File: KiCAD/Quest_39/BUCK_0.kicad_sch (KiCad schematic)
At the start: 32 parts, among them U4 AD626ANZ, U5 INA226, U6 LTM4611EV-PBF, U7 MCP4151-502E/SN

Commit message: Gave all INA226's unique addresses
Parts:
- renumbered C20 to C19, C21 to C20, C22 to C21, C23 to C22, C24 to C23, C25 to C24, C26 to C25, C27 to C26, C28 to C27, R6 to R17, R7 to R18, R8 to R19, R9 to R20, R10 to R21, R11 to R22, R12 to R23, TP7 to TP6, TP6 to TP7
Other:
- note added: "Addr=0x40"
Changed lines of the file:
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@@
   (junction (at 203.2 50.8) (diameter 0) (color 0 0 0 0)
+  )
+  (junction (at 363.22 172.72) (diameter 0) (color 0 0 0 0)
   )
   (junction (at 67.31 50.8) (diameter 0) (color 0 0 0 0)
@@
     (stroke (width 0) (type default) (color 0 0 0 0))
   )
-  (wire (pts (xy 356.87 172.72) (xy 370.84 172.72))
+  (wire (pts (xy 356.87 172.72) (xy 363.22 172.72))
     (stroke (width 0) (type default) (color 0 0 0 0))
   )
@@
     (stroke (width 0) (type default) (color 0 0 0 0))
   )
+  (wire (pts (xy 363.22 172.72) (xy 370.84 172.72))
+    (stroke (width 0) (type default) (color 0 0 0 0))
+  )
   (wire (pts (xy 233.68 215.9) (xy 236.22 215.9))
     (stroke (width 0) (type default) (color 0 0 0 0))
@@
   (polyline (pts (xy 13.97 43.18) (xy 87.63 43.18))
     (stroke (width 0) (type default) (color 0 0 0 0))
+  )
+  (text "Addr=0x40" (at 102.87 92.71 0)
+    (effects (font (size 1.27 1.27)) (justify left bottom))
   )
   (text "10:1 divider" (at 26.67 69.85 0)
@@
   (symbol (lib_id "Device:C") (at 25.4 93.98 0) (unit 1)
     (in_bom yes) (on_board yes) (fields_autoplaced)
-    (property "Reference" "C20" (id 0) (at 29.21 92.7099 0)
+    (property "Reference" "C19" (id 0) (at 29.21 92.7099 0)
       (effects (font (size 1.27 1.27)) (justify left))
     )
@@
   (symbol (lib_id "Device:R") (at 129.54 100.33 0) (unit 1)
     (in_bom yes) (on_board yes) (fields_autoplaced)
-    (property "Reference" "R11" (id 0) (at 132.08 99.0599 0)
+    (property "Reference" "R22" (id 0) (at 132.08 99.0599 0)
       (effects (font (size 1.27 1.27)) (justify left))
     )
@@
   (symbol (lib_id "power:GND") (at 21.59 86.36 0) (unit 1)
     (in_bom yes) (on_board yes)
-    (property "Reference" "#PWR011" (id 0) (at 21.59 92.71 0)
+    (property "Reference" "#PWR032" (id 0) (at 21.59 92.71 0)
       (effects (font (size 1.27 1.27)) hide)
     )
@@
   (symbol (lib_id "power:GND") (at 116.84 110.49 0) (unit 1)
     (in_bom yes) (on_board yes)
-    (property "Reference" "#PWR0113" (id 0) (at 116.84 116.84 0)
+    (property "Reference" "#PWR035" (id 0) (at 116.84 116.84 0)
       (effects (font (size 1.27 1.27)) hide)
     )
@@
   (symbol (lib_id "Device:R") (at 25.4 64.77 0) (unit 1)
     (in_bom yes) (on_board yes) (fields_autoplaced)
-    (property "Reference" "R9" (id 0) (at 27.94 63.4999 0)
+    (property "Reference" "R20" (id 0) (at 27.94 63.4999 0)
       (effects (font (size 1.27 1.27)) (justify left))
     )
@@
   (symbol (lib_id "power:+5V") (at 93.98 81.28 0) (unit 1)
     (in_bom yes) (on_board yes) (fields_autoplaced)
-    (property "Reference" "#PWR0110" (id 0) (at 93.98 85.09 0)
+    (property "Reference" "#PWR030" (id 0) (at 93.98 85.09 0)
       (effects (font (size 1.27 1.27)) hide)
     )
@@
   (symbol (lib_id "power:GND") (at 340.36 238.76 0) (unit 1)
     (in_bom yes) (on_board yes) (fields_autoplaced)
-    (property "Reference" "#PWR0114" (id 0) (at 340.36 245.11 0)
+    (property "Reference" "#PWR038" (id 0) (at 340.36 245.11 0)
       (effects (font (size 1.27 1.27)) hide)
     )
@@
   (symbol (lib_id "Connector:TestPoint") (at 234.95 53.34 0) (unit 1)
     (in_bom yes) (on_board yes)
-    (property "Reference" "TP7" (id 0) (at 234.95 48.26 0)
+    (property "Reference" "TP6" (id 0) (at 234.95 48.26 0)
       (effects (font (size 1.27 1.27)) (justify left))
     )
@@
   (symbol (lib_id "Device:R") (at 67.31 63.5 0) (unit 1)
     (in_bom yes) (on_board yes)
-    (property "Reference" "R7" (id 0) (at 68.58 62.23 0)
+    (property "Reference" "R18" (id 0) (at 68.58 62.23 0)
       (effects (font (size 1.27 1.27)) (justify left))
     )
@@
   (symbol (lib_id "power:+5V") (at 340.36 227.33 0) (unit 1)
     (in_bom yes) (on_board yes) (fields_autoplaced)
-    (property "Reference" "#PWR0115" (id 0) (at 340.36 231.14 0)
+    (property "Reference" "#PWR036" (id 0) (at 340.36 231.14 0)
       (effects (font (size 1.27 1.27)) hide)
     )
@@
   (symbol (lib_id "Device:R") (at 25.4 74.93 0) (unit 1)
     (in_bom yes) (on_board yes) (fields_autoplaced)
-    (property "Reference" "R10" (id 0) (at 27.94 73.6599 0)
+    (property "Reference" "R21" (id 0) (at 27.94 73.6599 0)
       (effects (font (size 1.27 1.27)) (justify left))
     )
@@
   (symbol (lib_id "power:+5V") (at 64.77 83.82 0) (unit 1)
     (in_bom yes) (on_board yes) (fields_autoplaced)
-    (property "Reference" "#PWR010" (id 0) (at 64.77 87.63 0)
+    (property "Reference" "#PWR031" (id 0) (at 64.77 87.63 0)
       (effects (font (size 1.27 1.27)) hide)
     )
@@
   (symbol (lib_id "Device:R") (at 82.55 63.5 0) (unit 1)
     (in_bom yes) (on_board yes)
-    (property "Reference" "R8" (id 0) (at 78.74 62.23 0)
+    (property "Reference" "R19" (id 0) (at 78.74 62.23 0)
       (effects (font (size 1.27 1.27)) (justify left))
     )
@@
   (symbol (lib_id "Device:C_Polarized") (at 370.84 179.07 0) (unit 1)
     (in_bom yes) (on_board yes)
-    (property "Reference" "C24" (id 0) (at 374.6295 177.7575 0)
+    (property "Reference" "C23" (id 0) (at 374.6295 177.7575 0)
       (effects (font (size 1.27 1.27)) (justify left))
     )
@@
   (symbol (lib_id "Device:C") (at 344.17 181.61 0) (unit 1)
     (in_bom yes) (on_board yes)
-    (property "Reference" "C27" (id 0) (at 346.71 180.34 0)
+    (property "Reference" "C26" (id 0) (at 346.71 180.34 0)
       (effects (font (size 1.27 1.27)) (justify left))
     )
@@
   (symbol (lib_id "Device:C_Polarized") (at 396.24 179.07 0) (unit 1)
     (in_bom yes) (on_board yes)
-    (property "Reference" "C26" (id 0) (at 400.0295 177.7575 0)
+    (property "Reference" "C25" (id 0) (at 400.0295 177.7575 0)
       (effects (font (size 1.27 1.27)) (justify left))
     )
@@
     (pin "1")
     (pin "2")
+  )
+  (symbol (lib_id "power:PWR_FLAG") (at 363.22 172.72 0) (unit 1)
+    (in_bom yes) (on_board yes) (fields_autoplaced)
+    (property "Reference" "#FLG0102" (id 0) (at 363.22 170.815 0)
+      (effects (font (size 1.27 1.27)) hide)
+    )
+    (property "Value" "PWR_FLAG" (id 1) (at 363.22 167.64 0))
+    (property "Footprint" "" (id 2) (at 363.22 172.72 0)
+      (effects (font (size 1.27 1.27)) hide)
+    )
+    (property "Datasheet" "~" (id 3) (at 363.22 172.72 0)
+      (effects (font (size 1.27 1.27)) hide)
+    )
+    (pin "1")
   )
   (symbol (lib_id "AD626ANZ:AD626ANZ") (at 5.08 80.01 0) (unit 1)
@@
   (symbol (lib_id "Connector:TestPoint") (at 77.47 100.33 180) (unit 1)
     (in_bom yes) (on_board yes)
-    (property "Reference" "TP6" (id 0) (at 78.74 102.87 0)
+    (property "Reference" "TP7" (id 0) (at 78.74 102.87 0)
       (effects (font (size 1.27 1.27)) (justify right))
     )
@@
   (symbol (lib_id "Device:C") (at 63.5 95.25 0) (unit 1)
     (in_bom yes) (on_board yes)
-    (property "Reference" "C21" (id 0) (at 57.15 93.98 0)
+    (property "Reference" "C20" (id 0) (at 57.15 93.98 0)
       (effects (font (size 1.27 1.27)) (justify left))
     )
@@
   (symbol (lib_id "power:GND") (at 285.75 238.76 0) (unit 1)
     (in_bom yes) (on_board yes) (fields_autoplaced)
-    (property "Reference" "#PWR0116" (id 0) (at 285.75 245.11 0)
+    (property "Reference" "#PWR037" (id 0) (at 285.75 245.11 0)
       (effects (font (size 1.27 1.27)) hide)
     )
@@
   (symbol (lib_id "Device:C_Polarized") (at 383.54 179.07 0) (unit 1)
     (in_bom yes) (on_board yes)
-    (property "Reference" "C25" (id 0) (at 387.3295 177.7575 0)
+    (property "Reference" "C24" (id 0) (at 387.3295 177.7575 0)
       (effects (font (size 1.27 1.27)) (justify left))
     )
@@
   (symbol (lib_id "power:GND") (at 25.4 99.06 0) (unit 1)
     (in_bom yes) (on_board yes)
-    (property "Reference" "#PWR012" (id 0) (at 25.4 105.41 0)
+    (property "Reference" "#PWR033" (id 0) (at 25.4 105.41 0)
       (effects (font (size 1.27 1.27)) hide)
     )
@@
   (symbol (lib_id "Device:C_Polarized") (at 356.87 179.07 0) (unit 1)
     (in_bom yes) (on_board yes)
-    (property "Reference" "C23" (id 0) (at 360.6595 177.7575 0)
+    (property "Reference" "C22" (id 0) (at 360.6595 177.7575 0)
       (effects (font (size 1.27 1.27)) (justify left))
     )
@@
   (symbol (lib_id "Device:R") (at 74.93 50.8 90) (unit 1)
     (in_bom yes) (on_board yes)
-    (property "Reference" "R6" (id 0) (at 74.93 45.72 90))
+    (property "Reference" "R17" (id 0) (at 74.93 45.72 90))
     (property "Value" "0R0025" (id 1) (at 74.93 48.26 90))
     (property "Footprint" "" (id 2) (at 74.93 52.578 90)
@@
   (symbol (lib_id "Device:C") (at 105.41 137.16 0) (unit 1)
     (in_bom yes) (on_board yes) (fields_autoplaced)
-    (property "Reference" "C22" (id 0) (at 109.22 135.8899 0)
+    (property "Reference" "C21" (id 0) (at 109.22 135.8899 0)
       (effects (font (size 1.27 1.27)) (justify left))
     )
@@
   (symbol (lib_id "Device:C") (at 340.36 233.68 0) (unit 1)
     (in_bom yes) (on_board yes) (fields_autoplaced)
-    (property "Reference" "C28" (id 0) (at 344.17 232.4099 0)
+    (property "Reference" "C27" (id 0) (at 344.17 232.4099 0)
       (effects (font (size 1.27 1.27)) (justify left))
     )
@@
   (symbol (lib_id "power:PWR_FLAG") (at 166.37 50.8 0) (unit 1)
     (in_bom yes) (on_board yes) (fields_autoplaced)
-    (property "Reference" "#FLG0101" (id 0) (at 166.37 48.895 0)
+    (property "Reference" "#FLG03" (id 0) (at 166.37 48.895 0)
       (effects (font (size 1.27 1.27)) hide)
     )
@@
   (symbol (lib_id "power:GND") (at 63.5 100.33 0) (unit 1)
     (in_bom yes) (on_board yes)
-    (property "Reference" "#PWR013" (id 0) (at 63.5 106.68 0)
+    (property "Reference" "#PWR034" (id 0) (at 63.5 106.68 0)
       (effects (font (size 1.27 1.27)) hide)
     )
@@
   (symbol (lib_id "Device:R") (at 325.12 224.79 0) (unit 1)
     (in_bom yes) (on_board yes) (fields_autoplaced)
-    (property "Reference" "R12" (id 0) (at 327.66 223.5199 0)
-      (effects (font (size 1.27 1.27)) (justify left))
-    )
+    (property "Reference" "R23" (id 0) (at 327.66 223.5199 0)
+      (effects (font (size 1.27 1.27)) (justify left))
+    )

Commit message: Removed all ERC errors
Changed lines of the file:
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@@
   (junction (at 203.2 50.8) (diameter 0) (color 0 0 0 0)
-  )
-  (junction (at 363.22 172.72) (diameter 0) (color 0 0 0 0)
   )
   (junction (at 67.31 50.8) (diameter 0) (color 0 0 0 0)
@@
     (stroke (width 0) (type default) (color 0 0 0 0))
   )
-  (wire (pts (xy 356.87 172.72) (xy 363.22 172.72))
+  (wire (pts (xy 356.87 172.72) (xy 370.84 172.72))
     (stroke (width 0) (type default) (color 0 0 0 0))
   )
@@
   )
   (wire (pts (xy 63.5 99.06) (xy 63.5 100.33))
-    (stroke (width 0) (type default) (color 0 0 0 0))
-  )
-  (wire (pts (xy 363.22 172.72) (xy 370.84 172.72))
     (stroke (width 0) (type default) (color 0 0 0 0))
   )
@@
     (pin "2")
   )
-  (symbol (lib_id "power:PWR_FLAG") (at 363.22 172.72 0) (unit 1)
-    (in_bom yes) (on_board yes) (fields_autoplaced)
-    (property "Reference" "#FLG0102" (id 0) (at 363.22 170.815 0)
-      (effects (font (size 1.27 1.27)) hide)
-    )
-    (property "Value" "PWR_FLAG" (id 1) (at 363.22 167.64 0))
-    (property "Footprint" "" (id 2) (at 363.22 172.72 0)
-      (effects (font (size 1.27 1.27)) hide)
-    )
-    (property "Datasheet" "~" (id 3) (at 363.22 172.72 0)
-      (effects (font (size 1.27 1.27)) hide)
-    )
-    (pin "1")
-  )
   (symbol (lib_id "AD626ANZ:AD626ANZ") (at 5.08 80.01 0) (unit 1)

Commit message: Assigned all schem. symbols their footprints
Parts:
- removed C22, C23, C24, C25: 100uF, symbol Device:C_Polarized
- added C22, C23, C24, C25: 100uF, Capacitor_SMD:C_1206_3216Metric, symbol Device:C
- C14: footprint (none) -> Capacitor_SMD:CP_Elec_8x6.9
- C15, C16, C17, C19, C20, C21, C26, C27: footprint (none) -> Capacitor_SMD:C_0805_2012Metric
- C18: footprint OptoDevice:R_LDR_4.9x4.2mm_P2.54mm_Vertical -> Capacitor_SMD:C_0805_2012Metric
- R17: footprint (none) -> Resistor_SMD:R_1206_3216Metric
- R18, R19, R20, R21, R22, R23: footprint (none) -> Resistor_SMD:R_0805_2012Metric
- TP10, TP11, TP12, TP6, TP7, TP8, TP9: footprint (none) -> TestPoint:TestPoint_Pad_D2.0mm
- U4: footprint N_8_ADI -> Package_DIP:DIP-8_W7.62mm_Socket_LongPads
- U6: footprint LGA-133_3_LIT -> Package_LGA:Linear_LGA-133_15.0x15.0mm_Layout12x12_P1.27mm
- U7: footprint SOIC8-N_MC_MCH -> Package_SO:MSOP-8_3x3mm_P0.65mm
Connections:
- net NEG: now also C22.2, C23.2, C24.2, C25.2
- net POS: now also C22.1, C23.1, C24.1, C25.1

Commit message: Initial work on layout
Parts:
- C18, C19, C20, C21, C26, C27: footprint Capacitor_SMD:C_0805_2012Metric -> Capacitor_SMD:C_0603_1608Metric
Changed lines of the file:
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@@
       (effects (font (size 1.27 1.27)) (justify left))
     )
-    (property "Footprint" "Capacitor_SMD:C_0805_2012Metric" (id 2) (at 26.3652 97.79 0)
+    (property "Footprint" "Capacitor_SMD:C_0603_1608Metric" (id 2) (at 26.3652 97.79 0)
       (effects (font (size 1.27 1.27)) hide)
     )
@@
       (effects (font (size 1.27 1.27)) (justify left))
     )
-    (property "Footprint" "Capacitor_SMD:C_0805_2012Metric" (id 2) (at 345.1352 185.42 0)
+    (property "Footprint" "Capacitor_SMD:C_0603_1608Metric" (id 2) (at 345.1352 185.42 0)
       (effects (font (size 1.27 1.27)) hide)
     )
@@
     (property "Reference" "C18" (id 0) (at 74.93 73.66 90))
     (property "Value" "1uF" (id 1) (at 74.93 81.28 90))
-    (property "Footprint" "Capacitor_SMD:C_0805_2012Metric" (id 2) (at 78.74 76.5048 0)
+    (property "Footprint" "Capacitor_SMD:C_0603_1608Metric" (id 2) (at 78.74 76.5048 0)
       (effects (font (size 1.27 1.27)) hide)
     )
@@
       (effects (font (size 1.27 1.27)) (justify left))
     )
-    (property "Footprint" "Capacitor_SMD:C_0805_2012Metric" (id 2) (at 64.4652 99.06 0)
+    (property "Footprint" "Capacitor_SMD:C_0603_1608Metric" (id 2) (at 64.4652 99.06 0)
       (effects (font (size 1.27 1.27)) hide)
     )
@@
       (effects (font (size 1.27 1.27)) (justify left))
     )
-    (property "Footprint" "Capacitor_SMD:C_0805_2012Metric" (id 2) (at 106.3752 140.97 0)
+    (property "Footprint" "Capacitor_SMD:C_0603_1608Metric" (id 2) (at 106.3752 140.97 0)
       (effects (font (size 1.27 1.27)) hide)
     )
@@
       (effects (font (size 1.27 1.27)) (justify left))
     )
-    (property "Footprint" "Capacitor_SMD:C_0805_2012Metric" (id 2) (at 341.3252 237.49 0)
-      (effects (font (size 1.27 1.27)) hide)
-    )
+    (property "Footprint" "Capacitor_SMD:C_0603_1608Metric" (id 2) (at 341.3252 237.49 0)
+      (effects (font (size 1.27 1.27)) hide)
+    )

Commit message: Fixed INA226 schem. mistake and further layout work
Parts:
- added C19: 100nF, Capacitor_SMD:C_0603_1608Metric, symbol Device:C
- renumbered C19 to C20, C20 to C21, C21 to C22, C22 to C23, C23 to C24, C24 to C25, C25 to C26, C26 to C27, C27 to C28
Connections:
- net +5V: now also C19.1
- net GND: now also C19.2
- net PV_POS: no longer C14.1, C15.1, C16.1, C17.1, R17.2, R19.1, R22.1, U6.A1 (VIN), U6.A2 (VIN), U6.A3 (VIN), U6.A4 (VIN), U6.A5 (VIN), U6.A6 (VIN), U6.B1 (VIN), U6.B2 (VIN), U6.B3 (VIN), U6.B4 (VIN), U6.B5 (VIN), U6.B6 (VIN), U6.C1 (VIN), U6.C2 (VIN), U6.C3 (VIN), U6.C4 (VIN), U6.C5 (VIN), U6.C6 (VIN)
- net Vin+: now also C18.2; no longer C18.1
- net Vin-: now also C18.1; no longer C18.2, TP7.1, U4.5 (OUT), U5.8 (Vbus)
- new net: TP7.1, U4.5 (OUT), U5.8 (Vbus)
- new net BUCK_VIN: C14.1, C15.1, C16.1, C17.1, R17.2, R19.1, R22.1, U6.A1 (VIN), U6.A2 (VIN), U6.A3 (VIN), U6.A4 (VIN), U6.A5 (VIN), U6.A6 (VIN), U6.B1 (VIN), U6.B2 (VIN), U6.B3 (VIN), U6.B4 (VIN), U6.B5 (VIN), U6.B6 (VIN), U6.C1 (VIN), U6.C2 (VIN), U6.C3 (VIN), U6.C4 (VIN), U6.C5 (VIN), U6.C6 (VIN)
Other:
- moved on the sheet: C18

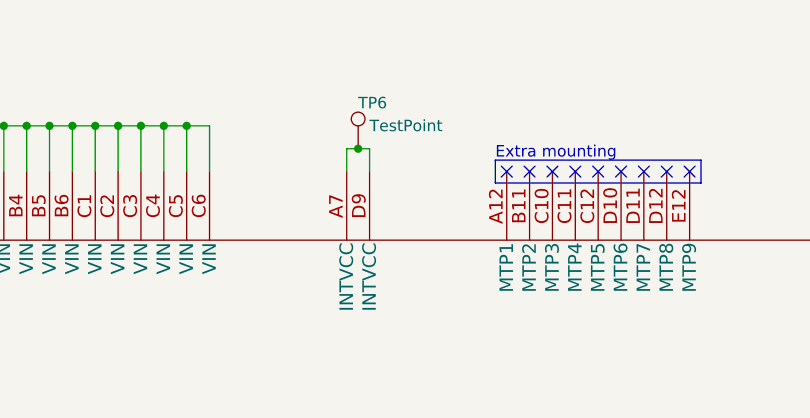
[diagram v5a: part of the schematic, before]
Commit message: Partial wiring of first buck converter section PCB layout
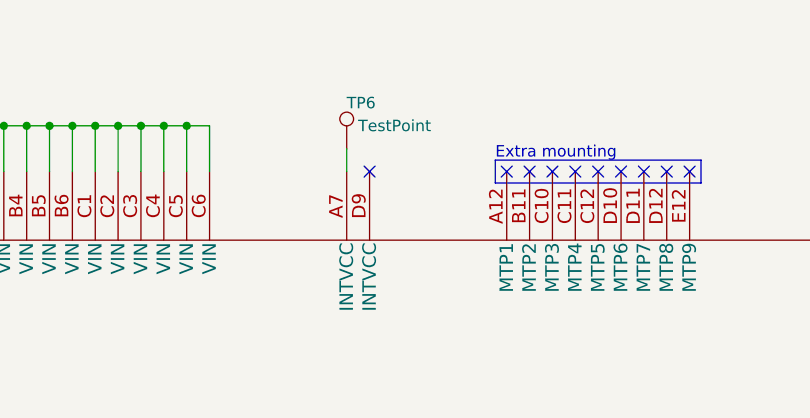
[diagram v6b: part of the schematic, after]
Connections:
- net at TP6.1, U6.A7 (INTVCC): no longer U6.D9 (INTVCC)
- no-connect marks 12 -> 13
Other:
- moved on the sheet: TP6
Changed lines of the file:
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@@
   (junction (at 130.81 50.8) (diameter 0) (color 0 0 0 0)
-  )
-  (junction (at 234.95 53.34) (diameter 0) (color 0 0 0 0)
   )
   (junction (at 279.4 215.9) (diameter 0) (color 0 0 0 0)
@@
   (no_connect (at 259.08 55.88))
   (no_connect (at 266.7 55.88))
+  (no_connect (at 236.22 55.88))
   (no_connect (at 261.62 55.88))
   (no_connect (at 251.46 55.88))
@@
     (stroke (width 0) (type default) (color 0 0 0 0))
   )
-  (wire (pts (xy 236.22 53.34) (xy 236.22 55.88))
-    (stroke (width 0) (type default) (color 0 0 0 0))
-  )
   (polyline (pts (xy 120.65 66.04) (xy 120.65 116.84))
     (stroke (width 0) (type default) (color 0 0 0 0))
@@
     (stroke (width 0) (type default) (color 0 0 0 0))
   )
-  (wire (pts (xy 233.68 53.34) (xy 234.95 53.34))
-    (stroke (width 0) (type default) (color 0 0 0 0))
-  )
   (wire (pts (xy 344.17 185.42) (xy 344.17 200.66))
     (stroke (width 0) (type default) (color 0 0 0 0))
@@
   )
   (wire (pts (xy 198.12 215.9) (xy 200.66 215.9))
-    (stroke (width 0) (type default) (color 0 0 0 0))
-  )
-  (wire (pts (xy 234.95 53.34) (xy 236.22 53.34))
     (stroke (width 0) (type default) (color 0 0 0 0))
   )
@@
     (pin "1")
   )
-  (symbol (lib_id "Connector:TestPoint") (at 234.95 53.34 0) (unit 1)
+  (symbol (lib_id "Connector:TestPoint") (at 233.68 53.34 0) (unit 1)
     (in_bom yes) (on_board yes)
-    (property "Reference" "TP6" (id 0) (at 234.95 48.26 0)
-      (effects (font (size 1.27 1.27)) (justify left))
-    )
-    (property "Value" "TestPoint" (id 1) (at 236.22 50.8 0)
-      (effects (font (size 1.27 1.27)) (justify left))
-    )
-    (property "Footprint" "TestPoint:TestPoint_Pad_D2.0mm" (id 2) (at 240.03 53.34 0)
-      (effects (font (size 1.27 1.27)) hide)
-    )
-    (property "Datasheet" "~" (id 3) (at 240.03 53.34 0)
-      (effects (font (size 1.27 1.27)) hide)
-    )
+    (property "Reference" "TP6" (id 0) (at 233.68 48.26 0)
+      (effects (font (size 1.27 1.27)) (justify left))
+    )
+    (property "Value" "TestPoint" (id 1) (at 234.95 50.8 0)
+      (effects (font (size 1.27 1.27)) (justify left))
+    )
+    (property "Footprint" "TestPoint:TestPoint_Pad_D2.0mm" (id 2) (at 238.76 53.34 0)
+      (effects (font (size 1.27 1.27)) hide)
+    )
+    (property "Datasheet" "~" (id 3) (at 238.76 53.34 0)
+      (effects (font (size 1.27 1.27)) hide)
+    )

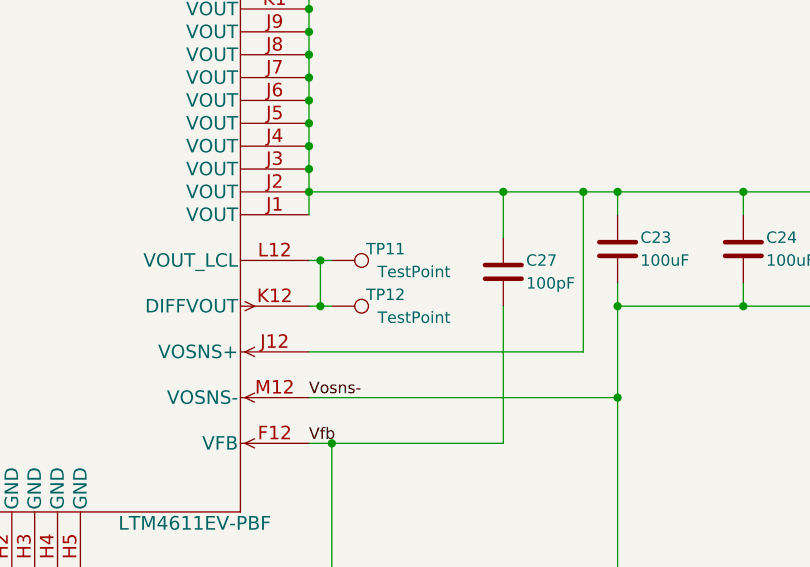
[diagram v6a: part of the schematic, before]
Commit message: Added 3rd buck converter section
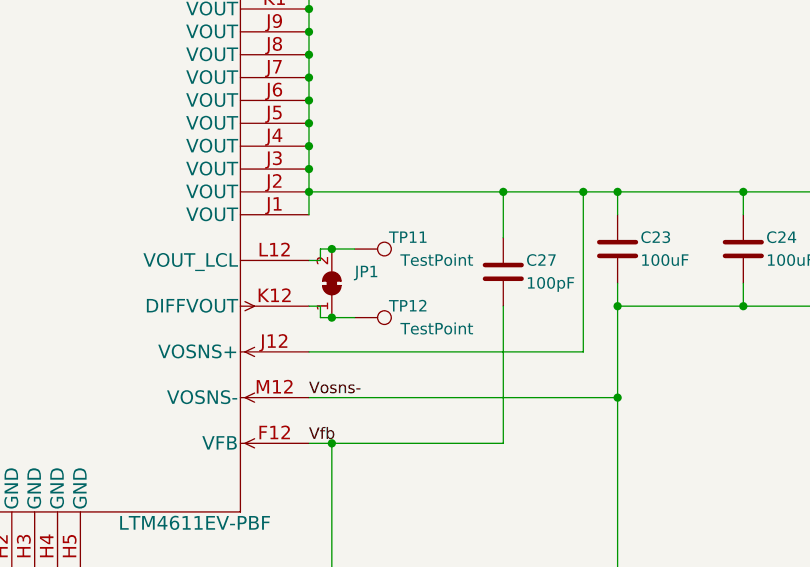
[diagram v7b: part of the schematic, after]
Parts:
- added JP1: SolderJumper_2_Bridged, Jumper:SolderJumper-2_P1.3mm_Bridged_RoundedPad1.0x1.5mm, symbol Jumper:SolderJumper_2_Bridged
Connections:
- net at TP12.1, U6.K12 (DIFFVOUT): now also JP1.1 (A); no longer TP11.1, U6.L12 (VOUT_LCL)
- new net: JP1.2 (B), TP11.1, U6.L12 (VOUT_LCL)
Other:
- moved on the sheet: TP11, TP12
